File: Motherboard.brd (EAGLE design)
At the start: 100 x 80 mm, 8 parts

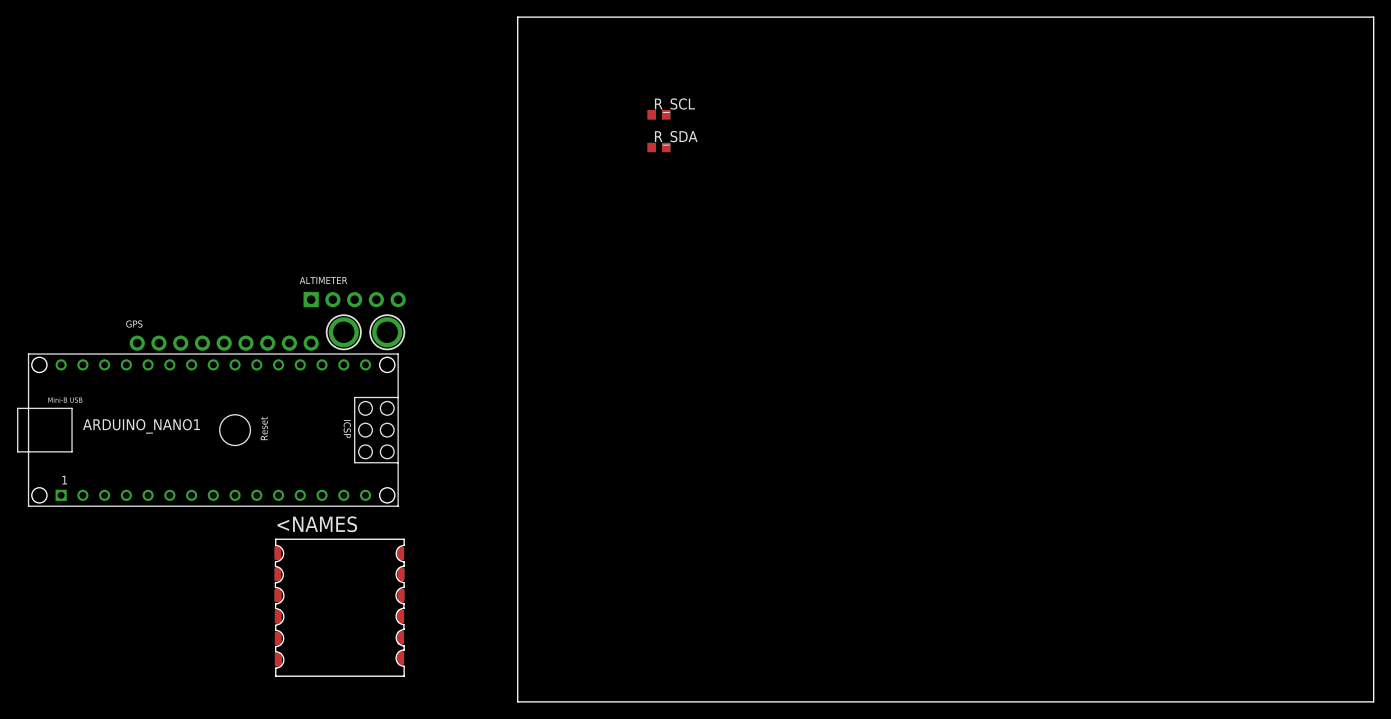
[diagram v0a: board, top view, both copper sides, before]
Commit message: add buck converter
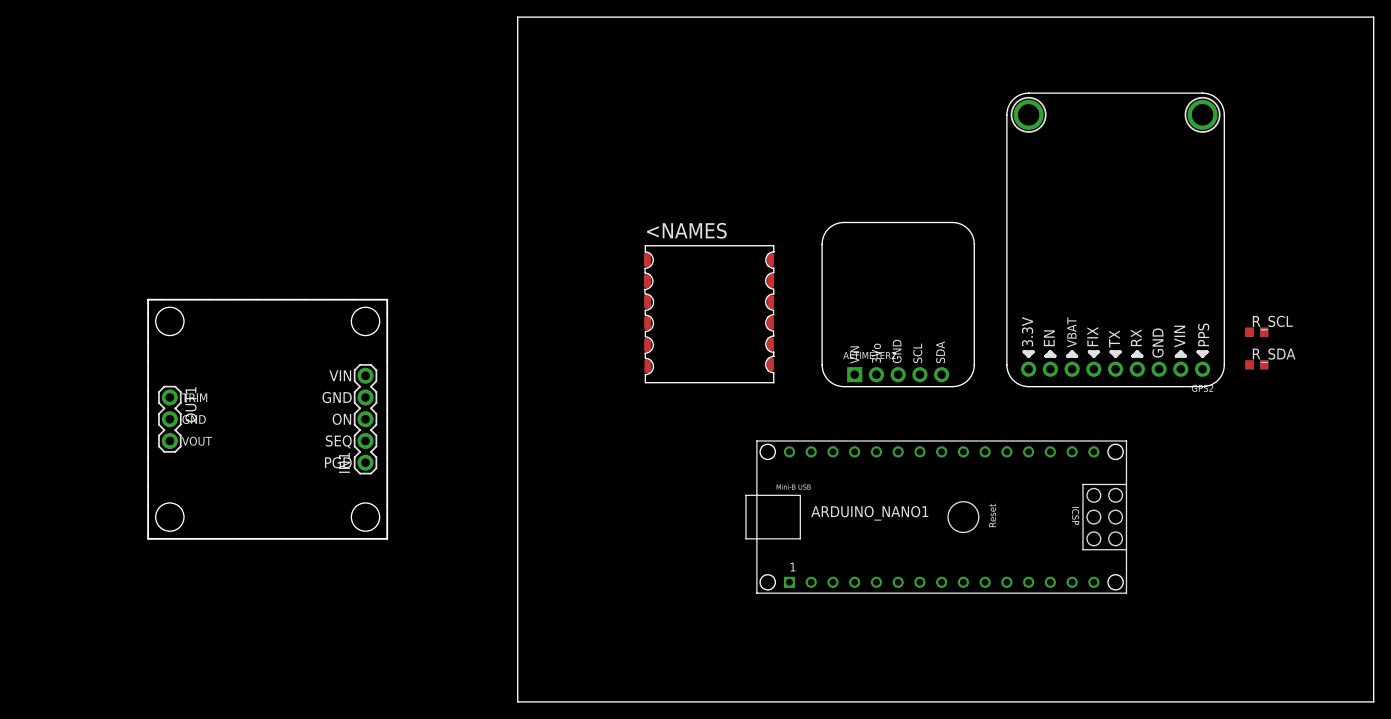
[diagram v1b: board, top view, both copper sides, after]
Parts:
- removed ALTIMETER: (no value), microbuilder:1X05_ROUND_70
- removed GPS: (no value), microbuilder:1X09_ROUND_70
- added ALTIMETER2: (no value), microbuilder:1X05_ROUND_70
- added GPS2: (no value), microbuilder:1X09_ROUND_70
- added IN1: (no value), SparkFun:1X05
- added OUT1: (no value), SparkFun:1X03
- added U$10, U$7: STAND-OFF, SparkFun:STAND-OFF
- added U$3, U$4: MOUNTINGHOLE2.5, microbuilder:MOUNTINGHOLE_2.5_PLATED
- U$8, U$9: value MOUNTINGHOLE2.5 -> STAND-OFF; device microbuilder:MOUNTINGHOLE_2.5_PLATED -> SparkFun:STAND-OFF
- moved ARDUINO_NANO1 85.7 mm to (52.1, 21.6)
- moved R_SCL 74.3 mm to (86.4, 43.2)
- moved R_SDA 74.3 mm to (86.4, 39.4)
- moved IMU 55.1 mm to (12.7, 44.5)
- moved U$9 29.6 mm to (-40.6, 21.6), turned to 90 degrees
- moved U$8 2.84 mm to (-17.8, 44.5), turned to 90 degrees
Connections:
- new net ON/OFF: IN1.3
- new net PGOOD: IN1.1
- new net SEQ: IN1.2
- new net TRIM: OUT1.1
- new net VOUT: OUT1.3
- net 3V3: now also ALTIMETER2.1, GPS2.1; no longer ALTIMETER.1, GPS.1
- net GND: now also ALTIMETER2.3, GPS2.7, IN1.4, OUT1.2; no longer ALTIMETER.3, GPS.7
- net RX: now also GPS2.5; no longer GPS.5
- net SCL: now also ALTIMETER2.4; no longer ALTIMETER.4
- net SDA: now also ALTIMETER2.5; no longer ALTIMETER.5
- net TX: now also GPS2.6; no longer GPS.6
- net VIN: now also IN1.5
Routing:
- added copper zone on layer 1, net GND
- added copper zone on layer 16, net GND
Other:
- board size 100 x 80 mm -> 143.2 x 80 mm
- board text added: "3.3V"
- board text added: "3Vo"
- board text added: "EN"
- board text added: "FIX"
- board text added: "GND"
- board text added: "ON"
- board text added: "PGD"
- board text added: "PPS"
- board text added: "RX"
- board text added: "SCL"
- board text added: "SDA"
- board text added: "SEQ"
- board text added: "TRIM"
- board text added: "TX"
- board text added: "VBAT"
- board text added: "VIN"
- board text added: "VOUT"

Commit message: test
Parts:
- added R_TRIM: (no value), rcl:R0603
- moved U$9 117.1 mm to (66.0, 69.8), turned to 270 degrees
- moved OUT1 108.6 mm to (66.0, 55.9), turned to 90 degrees
- moved U$10 106.7 mm to (66.0, 47.0), turned to 270 degrees
- moved U$7 77.8 mm to (43.2, 69.8), turned to 270 degrees
- moved IN1 70.6 mm to (43.2, 63.5), turned to 270 degrees
- moved U$8 61.0 mm to (43.2, 47.0), turned to 270 degrees
- moved R_SCL 30.9 mm to (91.4, 12.7)
- moved R_SDA 30.9 mm to (91.4, 8.89)
- moved GPS2 21.6 mm to (85.1, 23.6)
- moved IMU 21.6 mm to (27.9, 29.2)
- moved U$3 21.6 mm to (74.9, 53.3)
- moved ALTIMETER2 21.6 mm to (59.7, 23.0)
- moved U$4 21.6 mm to (95.2, 53.3)
- moved ARDUINO_NANO1 19.1 mm to (67.3, 10.2)
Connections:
- removed net VOUT: OUT1.3
- new net GND_BATT: IN1.4
- new net V_BATT: IN1.5
- net GND: now also R_TRIM.1; no longer IN1.4
- net TRIM: now also R_TRIM.2
- net VIN: now also OUT1.3; no longer IN1.5
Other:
- board size 143.2 x 80 mm -> 100 x 80 mm

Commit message: more circuit
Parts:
- added U$1: (no value), ArduinoNanoV30:RADIO
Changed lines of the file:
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@@
 <attribute name="SPICEPREFIX" value="R" x="91.44" y="5.08" size="1.778" layer="27" display="off"/>
 </element>
+<element name="U$1" library="ArduinoNanoV30" package="RADIO" value="" x="-17.78" y="49.53" rot="R90"/>
 </elements>
 <signals>
